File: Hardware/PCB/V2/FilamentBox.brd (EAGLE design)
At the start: 58.3 x 44.5 mm, 29 parts, among them IC1 7805TV, Q1 BC817, Q2 NX2301P, Q3 BC817, U3 PHOTON

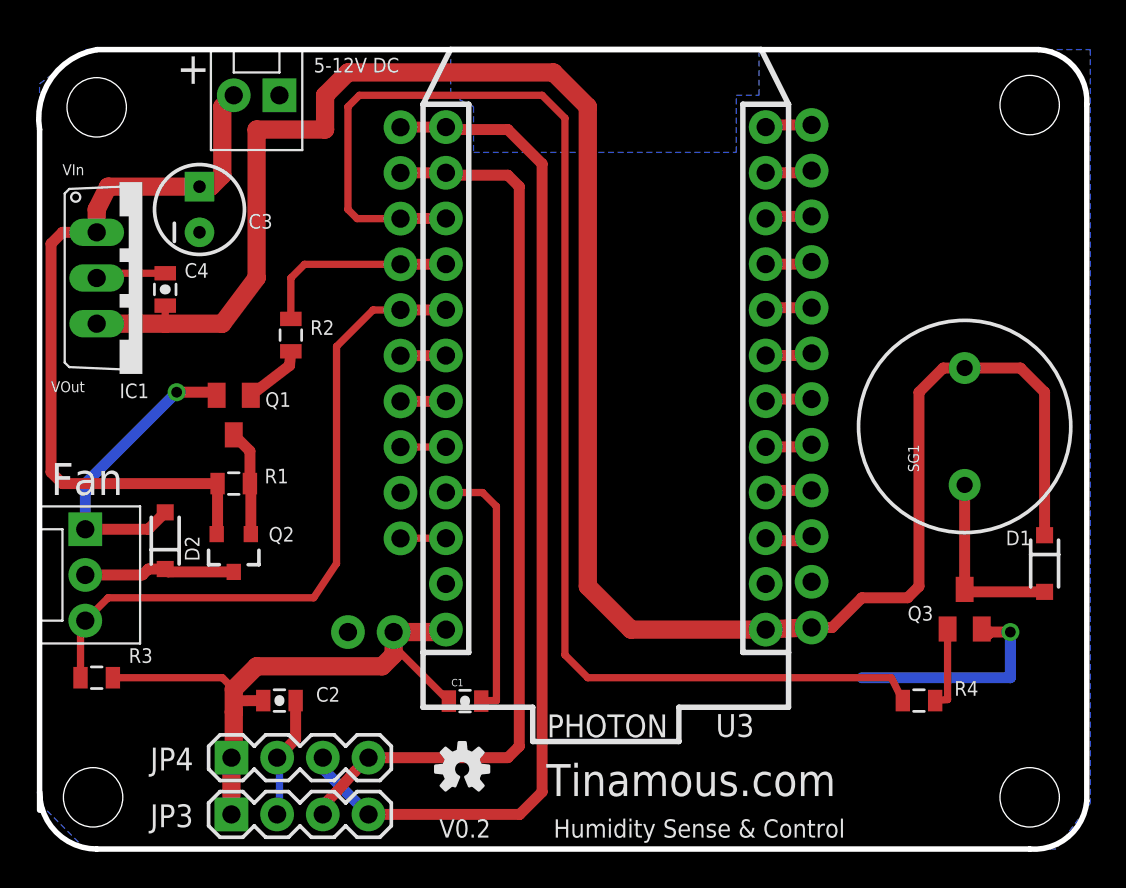
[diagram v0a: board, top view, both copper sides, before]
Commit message: Update (to 2.04)- Added reverse mount LEDs (Red, Yellow and Green for Humidity warning, fan status and OK (with OSH Logo)). Added poly fuse and diode for input protection. Swapped orientation of VIn connector and voltage regulator for better layout. Added PCB images generated by DirtyPCBs (note text is wrong way around).
Sent to DirtyPCBs (3-Jan-2017)
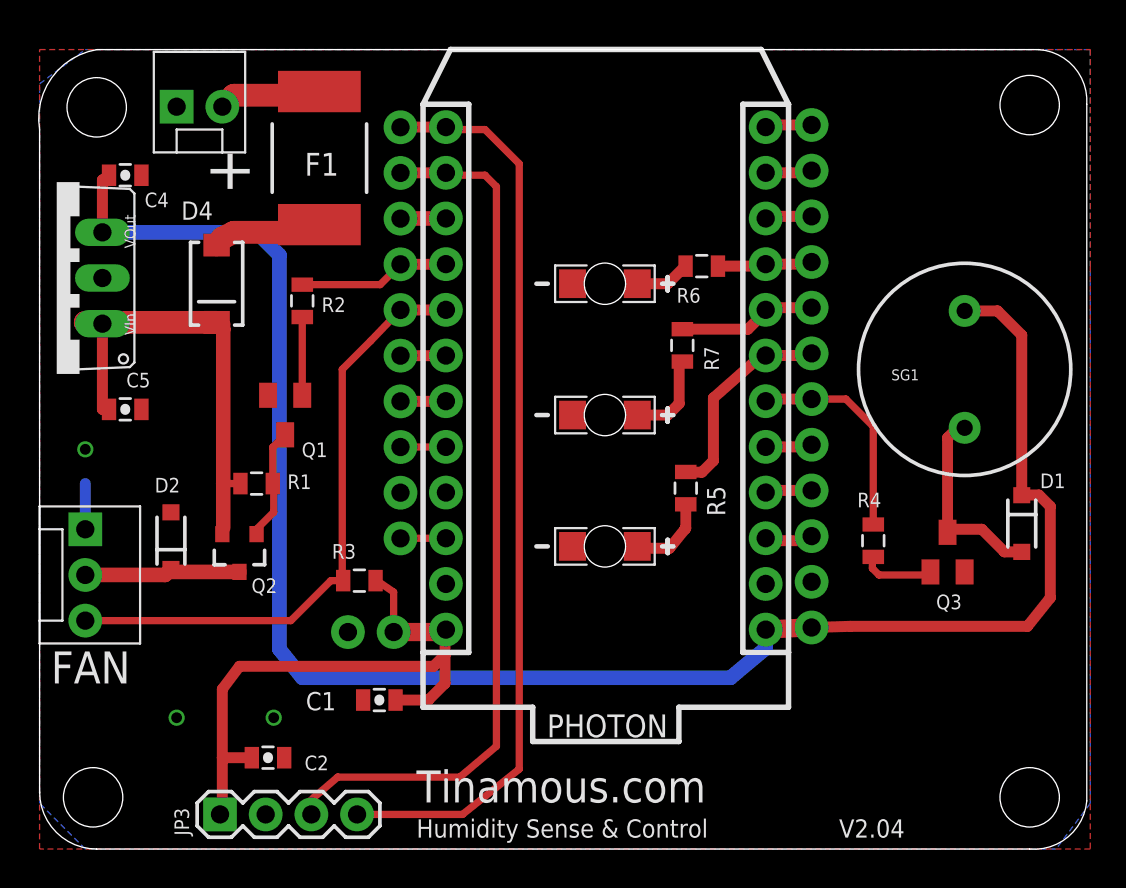
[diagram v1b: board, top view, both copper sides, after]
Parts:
- removed C3: 10uF, SparkFun-Capacitors:CPOL-RADIAL-10UF-25V
- removed JP4: (no value), SparkFun-Connectors:1X04
- added C5: 0.1uF 25V, SparkFun-Capacitors:0805-CAP
- added D3: Green, SparkFun-LED:LED-1206-BOTTOM
- added D4: MBRA140, SparkFun-DiscreteSemi:SMA-DIODE
- added D7: Red, SparkFun-LED:LED-1206-BOTTOM
- added D8: Yellow, SparkFun-LED:LED-1206-BOTTOM
- added F1: SMD100F/33, switch-raychem:SMD050F
- added FRAME1: FRAME-LETTER, SparkFun-Aesthetics:CREATIVE_COMMONS
- added R5, R6, R7: 1k5, SparkFun-Resistors:0805
- C4: value 1uF -> 0.1uF 10V
- LOGO1: value OSHW-LOGOS -> OSHW-LOGOL; device Spark:OSHW-LOGO-S -> Spark:OSHW-LOGO-L
- moved R3 15.6 mm to (17.8, 15.6)
- moved LOGO1 14.7 mm to (31.4, 17.5), flipped to the bottom
- moved R4 9.25 mm to (46.4, 17.8), turned to 90 degrees
- moved C4 6.73 mm to (4.76, 38.1), turned to 0 degrees
- moved JP1 5.75 mm to (7.62, 41.9), turned to 0 degrees
- moved C1 4.77 mm to (18.9, 8.92), turned to 180 degrees
- moved IC1 4.76 mm to (0.95, 32.4), turned to 90 degrees
- moved Q3 3.31 mm to (50.5, 17.1)
- moved C2 3.24 mm to (12.7, 5.71)
- moved SG1 3.18 mm to (51.4, 27.3)
- moved Q1 2.86 mm to (13.7, 24.8)
- moved D1 2.56 mm to (54.6, 18.7)
- moved R2 2.01 mm to (14.6, 31.1)
- moved R1 1.27 mm to (12.1, 21.0)
- moved JP3 0.63 mm to (10.0, 2.56)
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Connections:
- removed net N$7: JP5.4, U3.9
- removed net N$8: JP5.5, U3.8
- removed net N$9: JP5.6, U3.7
- new net FAN_LED: JP5.5, R7.2, U3.8
- new net HIGH_HUMIDITY_LED: JP5.4, R6.2, U3.9
- new net N$18: D3.A, R5.1
- new net N$19: F1.1, JP1.2
- new net N$20: D4.A, F1.2
- new net N$25: D7.A, R6.1
- new net N$26: D8.A, R7.1
- new net OSH_LED: JP5.6, R5.2, U3.7
- net 3.3V: no longer JP4.1
- net BUZZER: now also JP5.7, U3.6; no longer JP9.8, U3.15
- net GND: now also C5.2, D3.C, D7.C, D8.C; no longer C3.2, JP4.2
- net N$10: now also JP9.8, U3.15; no longer JP5.7, U3.6
- net SCL: no longer JP4.4
- net SDA: no longer JP4.3
- net VIN: now also C5.1, D4.C; no longer C3.1, JP1.2
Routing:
- net BUZZER: track 74.2 -> 12.1 mm
- net GND: track 55.0 -> 2.54 mm, vias 2 -> 3
- net 5V: track 114.9 -> 101.7 mm
- net VIN: track 41.9 -> 29.3 mm
- net OSH_LED: track 0.00 -> 11.7 mm
- net FAN_LED: track 0.00 -> 7.86 mm
- net SDA: track 58.0 -> 51.0 mm
- net N$20: track 0.00 -> 6.15 mm
- net N$19: track 0.00 -> 5.75 mm
- net HIGH_HUMIDITY_LED: track 0.00 -> 5.30 mm
- net N$26: track 0.00 -> 5.00 mm
- net N$18: track 0.00 -> 4.60 mm
- net PULSE: track 37.8 -> 34.2 mm
- net N$25: track 0.00 -> 3.09 mm
- net FAN_CONTROL: track 11.2 -> 8.46 mm
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- added copper zone on layer 1, net GND
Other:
- outline, holes or cut-outs redrawn
- board text added: "12V DC"
- board text added: "FAN"
- board text added: "High"
- board text added: "Humidity"
- board text added: "S.Harrison 3 Jan 2017"
- board text added: "V2.04"
- board text added: "https://github.com/Tinamous/HumidityMonitor"
- board text removed: "5-12V DC"
- board text removed: "V0.2"
